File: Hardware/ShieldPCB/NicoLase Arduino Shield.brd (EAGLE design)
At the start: 54.3 x 62.2 mm, 19 parts, among them IC1 4050D, J1 ARDUINO_R3_SHIELD, U1 7432SE

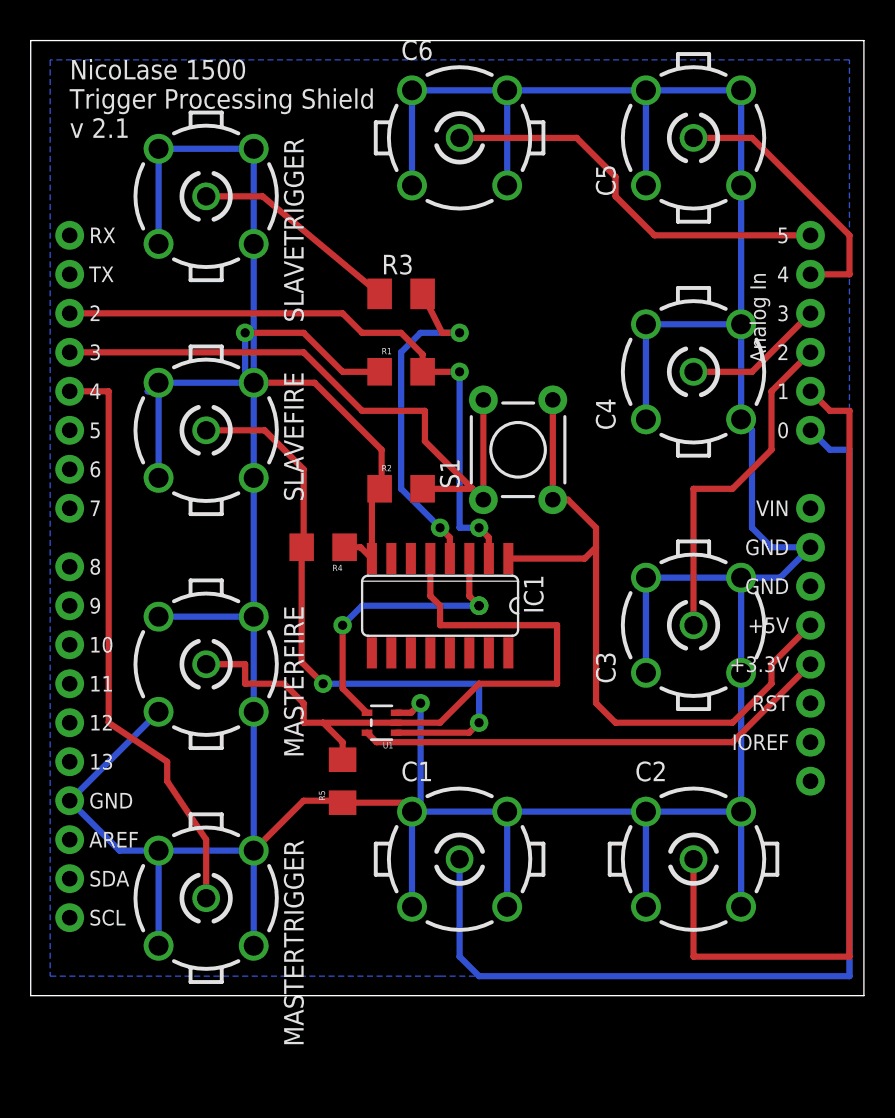
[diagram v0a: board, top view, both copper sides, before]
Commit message: Added ground plane and corrected minor layout issues.
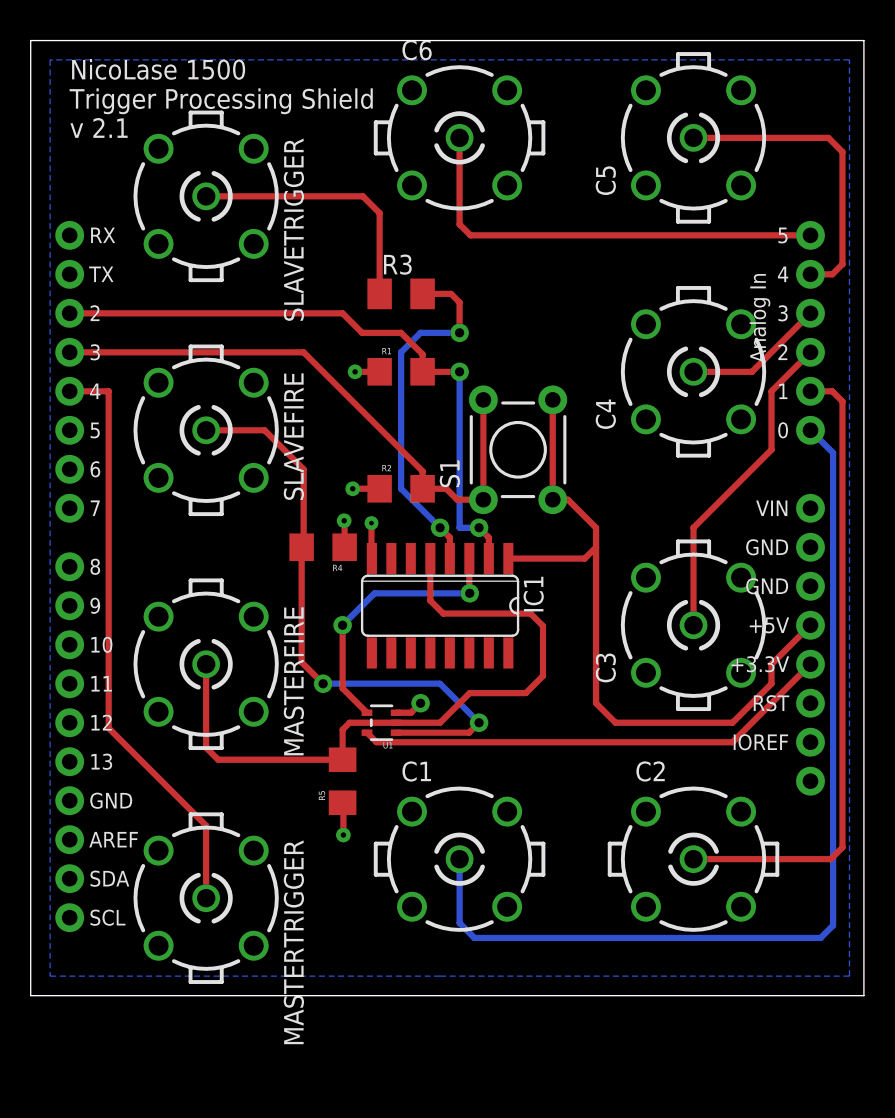
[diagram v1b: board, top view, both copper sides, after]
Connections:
- net N$2 renamed GND
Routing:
- net GND: track 331.7 -> 12.5 mm, vias 2 -> 6
- net N$4: track 55.1 -> 41.4 mm
- net N$3: track 69.6 -> 62.1 mm
- net N$13: track 42.8 -> 38.1 mm
- net N$11: track 13.6 -> 17.0 mm
- net N$8: track 26.2 -> 28.8 mm
- net N$7: track 17.9 -> 19.8 mm
- net N$26: track 40.4 -> 38.9 mm
- net N$5: track 22.4 -> 20.9 mm
- net N$10: track 19.1 -> 17.8 mm
- net SLAVEFIRE: track 46.0 -> 45.1 mm
- net N$15: track 23.1 -> 23.7 mm
- added copper zone on layer 16, net GND
- removed copper zone on layer 16, net N$20

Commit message: Added 0.1uF capacitors on power rails. Correcter minor schematic issues.
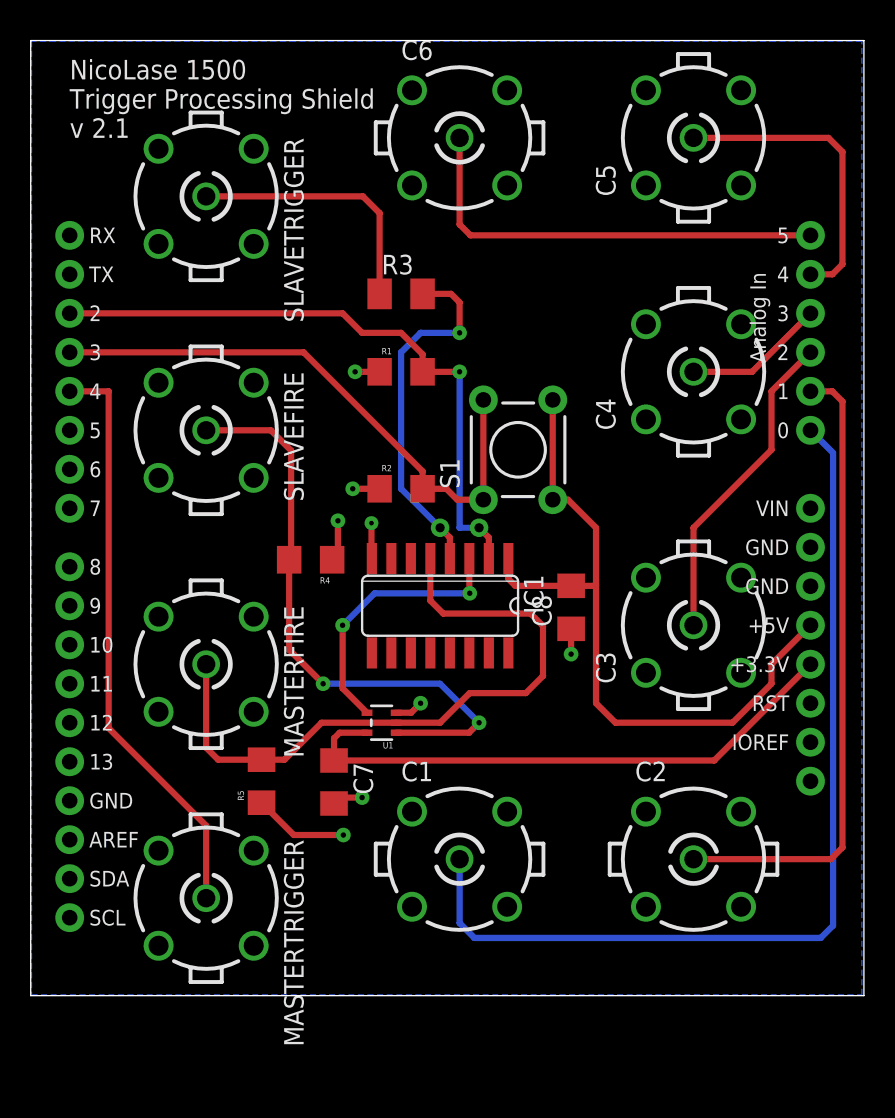
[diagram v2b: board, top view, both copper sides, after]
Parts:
- added C7, C8: 0.1uF, rcl:C1206
- moved R5 5.28 mm to (18.8, 21.6)
- moved R4 1.15 mm to (22.0, 36.0)
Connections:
- net GND: now also C7.2, C8.1
- net N$1: now also C7.1
- net N$16: now also C8.2
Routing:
- net GND: track 12.5 -> 21.1 mm, vias 6 -> 8
- net N$1: track 31.3 -> 37.4 mm
- net N$16: track 46.7 -> 48.0 mm
- net SLAVEFIRE: track 45.1 -> 44.0 mm

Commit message: Updated top silk.
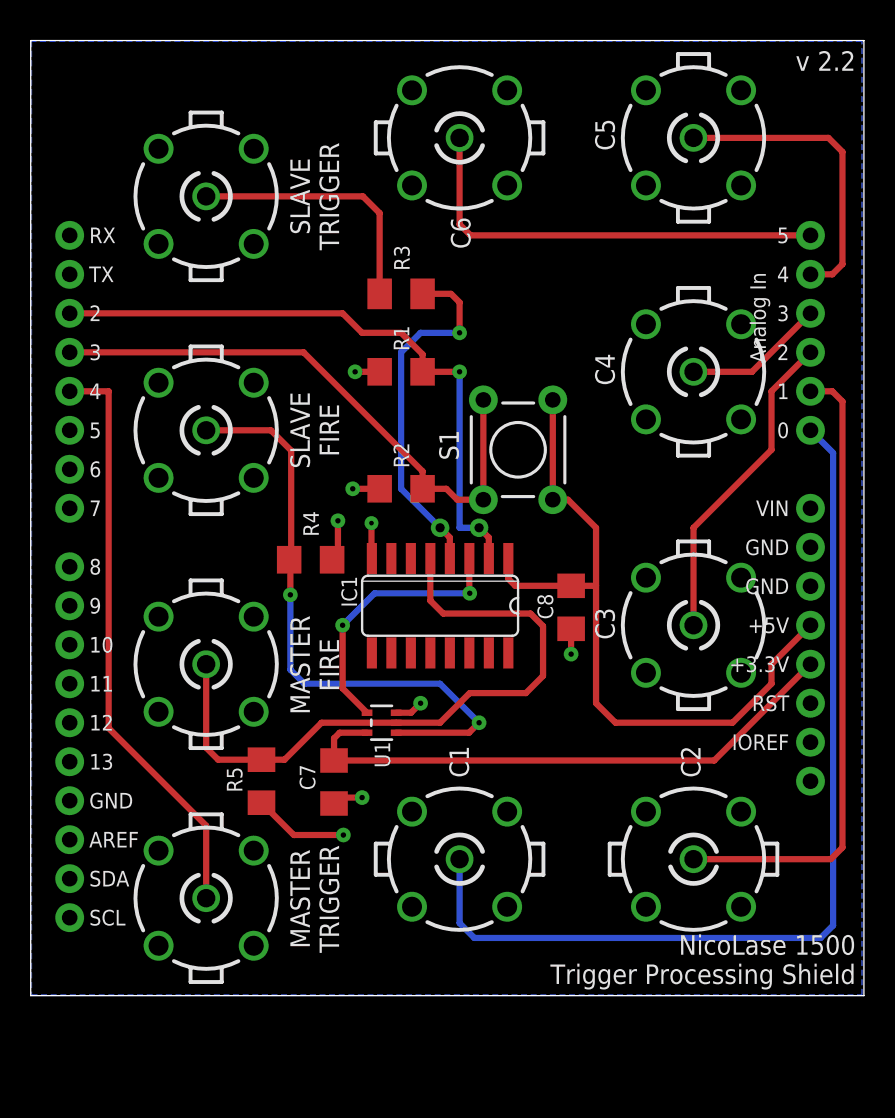
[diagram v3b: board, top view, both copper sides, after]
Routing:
- net N$26: track 39.1 -> 39.9 mm
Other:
- board text added: "MASTER FIRE"
- board text added: "MASTER TRIGGER"
- board text added: "NicoLase 1500 Trigger Processing Shield"
- board text added: "SLAVE FIRE"
- board text added: "SLAVE TRIGGER"
- board text added: "v 2.2"
- board text removed: "NicoLase 1500 Trigger Processing Shield v 2.1"

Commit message: Review filcarv pull request.  Update silkscreen and README terminology for primary/secondary fire/trigger lines.
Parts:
- renumbered MASTERFIRE to PRIMARYFIRE, MASTERTRIGGER to PRIMARYTRIGGER, SLAVEFIRE to 2NDARYFIRE, SLAVETRIGGER to 2NDARYTRIGGER
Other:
- board text added: "PRIMARY FIRE"
- board text added: "PRIMARY TRIGGER"
- board text added: "SECONDARY FIRE"
- board text added: "SECONDARY TRIGGER"
- board text removed: "MASTER FIRE"
- board text removed: "MASTER TRIGGER"
- board text removed: "SLAVE FIRE"
- board text removed: "SLAVE TRIGGER"
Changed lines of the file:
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@@
 <?xml version="1.0" encoding="utf-8"?>
 <!DOCTYPE eagle SYSTEM "eagle.dtd">
-<eagle version="9.5.1">
+<eagle version="9.0.1">
 <drawing>
 <settings>
@@
 <text x="57.5564" y="8.382" size="1.27" layer="21" font="vector" ratio="12" align="bottom-right">NicoLase 1500
 Trigger Processing Shield</text>
-<text x="20.7264" y="13.9192" size="1.27" layer="21" font="vector" ratio="15" rot="R90" align="top-center">MASTER
+<text x="20.7264" y="13.9192" size="1.27" layer="21" font="vector" ratio="15" rot="R90" align="top-center">PRIMARY
 TRIGGER</text>
-<text x="20.7264" y="29.1592" size="1.27" layer="21" font="vector" ratio="15" rot="R90" align="top-center">MASTER
+<text x="20.7264" y="29.1592" size="1.27" layer="21" font="vector" ratio="15" rot="R90" align="top-center">PRIMARY
 FIRE</text>
-<text x="20.7264" y="44.45" size="1.27" layer="21" font="vector" ratio="15" rot="R90" align="top-center">SLAVE
+<text x="20.7264" y="44.45" size="1.27" layer="21" font="vector" ratio="15" rot="R90" align="top-center">SECONDARY
 FIRE</text>
-<text x="20.7264" y="59.69" size="1.27" layer="21" font="vector" ratio="15" rot="R90" align="top-center">SLAVE
+<text x="20.7264" y="59.69" size="1.27" layer="21" font="vector" ratio="15" rot="R90" align="top-center">SECONDARY
 TRIGGER</text>
 <text x="57.5564" y="67.8688" size="1.27" layer="21" font="vector" ratio="12" align="bottom-right">v 2.2</text>
@@
 <param name="checkStop" value="0"/>
 <param name="checkValues" value="0"/>
-<param name="checkNames" value="1"/>
-<param name="checkWireStubs" value="1"/>
-<param name="checkPolygonWidth" value="0"/>
 <param name="useDiameter" value="13"/>
 <param name="maxErrors" value="50"/>
@@
 <attribute name="VALUE" x="34.544" y="33.655" size="1.27" layer="27" ratio="10" rot="R180"/>
 </element>
-<element name="MASTERFIRE" library="con-coax" package="B35N61" value="BN35N61" x="15.24" y="29.21" smashed="yes" rot="R270">
+<element name="PRIMARYFIRE" library="con-coax" package="B35N61" value="BN35N61" x="15.24" y="29.21" smashed="yes" rot="R270">
 <attribute name="MF" value="" x="15.24" y="29.21" size="1.778" layer="27" rot="R270" display="off"/>
 <attribute name="MPN" value="" x="15.24" y="29.21" size="1.778" layer="27" rot="R270" display="off"/>
@@
 <attribute name="NAME" x="30.4292" y="43.4848" size="1.27" layer="25" font="vector" ratio="15" rot="R270" align="bottom-center"/>
 </element>
-<element name="SLAVEFIRE" library="con-coax" package="B35N61" value="BN35N61" x="15.24" y="44.45" smashed="yes" rot="R270">
+<element name="2NDARYFIRE" library="con-coax" package="B35N61" value="BN35N61" x="15.24" y="44.45" smashed="yes" rot="R270">
 <attribute name="MF" value="" x="15.24" y="44.45" size="1.778" layer="27" rot="R270" display="off"/>
 <attribute name="MPN" value="" x="15.24" y="44.45" size="1.778" layer="27" rot="R270" display="off"/>
@@
 <attribute name="VALUE" x="8.89" y="48.26" size="1.27" layer="27" rot="R270"/>
 </element>
-<element name="SLAVETRIGGER" library="con-coax" package="B35N61" value="BN35N61" x="15.24" y="59.69" smashed="yes" rot="R270">
+<element name="2NDARYTRIGGER" library="con-coax" package="B35N61" value="BN35N61" x="15.24" y="59.69" smashed="yes" rot="R270">
 <attribute name="MF" value="" x="15.24" y="59.69" size="1.778" layer="27" rot="R270" display="off"/>
 <attribute name="MPN" value="" x="15.24" y="59.69" size="1.778" layer="27" rot="R270" display="off"/>
@@
 <attribute name="VALUE" x="27.432" y="27.051" size="0.4064" layer="27" rot="R180"/>
 </element>
-<element name="MASTERTRIGGER" library="con-coax" package="B35N61" value="BN35N61" x="15.24" y="13.97" smashed="yes" rot="R270">
+<element name="PRIMARYTRIGGER" library="con-coax" package="B35N61" value="BN35N61" x="15.24" y="13.97" smashed="yes" rot="R270">
 <attribute name="MF" value="" x="15.24" y="13.97" size="1.778" layer="27" rot="R270" display="off"/>
 <attribute name="MPN" value="" x="15.24" y="13.97" size="1.778" layer="27" rot="R270" display="off"/>
@@
 <contactref element="R5" pad="2"/>
 <contactref element="IC1" pad="5"/>
-<contactref element="MASTERFIRE" pad="1"/>
+<contactref element="PRIMARYFIRE" pad="1"/>
 <wire x1="30.48" y1="25.4" x2="32.4104" y2="27.3304" width="0.4064" layer="1"/>
 <wire x1="27.62" y1="25.4" x2="22.7584" y2="25.4" width="0.4064" layer="1"/>
@@
 <signal name="GND">
 <contactref element="IC1" pad="8"/>
-<contactref element="SLAVETRIGGER" pad="2"/>
-<contactref element="SLAVETRIGGER" pad="3"/>
-<contactref element="SLAVETRIGGER" pad="4"/>
-<contactref element="SLAVETRIGGER" pad="5"/>
-<contactref element="SLAVEFIRE" pad="2"/>
-<contactref element="SLAVEFIRE" pad="3"/>
-<contactref element="SLAVEFIRE" pad="4"/>
-<contactref element="SLAVEFIRE" pad="5"/>
-<contactref element="MASTERFIRE" pad="2"/>
-<contactref element="MASTERFIRE" pad="3"/>
-<contactref element="MASTERFIRE" pad="4"/>
-<contactref element="MASTERFIRE" pad="5"/>
+<contactref element="2NDARYTRIGGER" pad="2"/>
+<contactref element="2NDARYTRIGGER" pad="3"/>
+<contactref element="2NDARYTRIGGER" pad="4"/>
+<contactref element="2NDARYTRIGGER" pad="5"/>
+<contactref element="2NDARYFIRE" pad="2"/>
+<contactref element="2NDARYFIRE" pad="3"/>
+<contactref element="2NDARYFIRE" pad="4"/>
+<contactref element="2NDARYFIRE" pad="5"/>
+<contactref element="PRIMARYFIRE" pad="2"/>
+<contactref element="PRIMARYFIRE" pad="3"/>
+<contactref element="PRIMARYFIRE" pad="4"/>
+<contactref element="PRIMARYFIRE" pad="5"/>
 <contactref element="U1" pad="3"/>
 <contactref element="R1" pad="1"/>
@@
 <contactref element="C2" pad="5"/>
 <contactref element="C2" pad="2"/>
-<contactref element="MASTERTRIGGER" pad="4"/>
-<contactref element="MASTERTRIGGER" pad="3"/>
-<contactref element="MASTERTRIGGER" pad="5"/>
-<contactref element="MASTERTRIGGER" pad="2"/>
+<contactref element="PRIMARYTRIGGER" pad="4"/>
+<contactref element="PRIMARYTRIGGER" pad="3"/>
+<contactref element="PRIMARYTRIGGER" pad="5"/>
+<contactref element="PRIMARYTRIGGER" pad="2"/>
 <contactref element="J1" pad="GND@2"/>
 <contactref element="J1" pad="GND@1"/>
@@
 </signal>
 <signal name="N$11">
-<contactref element="SLAVETRIGGER" pad="1"/>
+<contactref element="2NDARYTRIGGER" pad="1"/>
 <contactref element="R3" pad="1"/>
 <wire x1="26.54" y1="58.6008" x2="26.54" y2="53.34" width="0.4064" layer="1"/>
@@
 </signal>
 <signal name="N$19">
-<contactref element="MASTERTRIGGER" pad="1"/>
+<contactref element="PRIMARYTRIGGER" pad="1"/>
 <contactref element="J1" pad="D4"/>
 <wire x1="6.35" y1="46.99" x2="8.89" y2="46.99" width="0.4064" layer="1"/>
@@
 <contactref element="R4" pad="2"/>
 <contactref element="U1" pad="1"/>
-<contactref element="SLAVEFIRE" pad="1"/>
+<contactref element="2NDARYFIRE" pad="1"/>
 <wire x1="15.24" y1="44.45" x2="19.4564" y2="44.45" width="0.4064" layer="1"/>
 <wire x1="19.4564" y1="44.45" x2="20.7772" y2="43.1292" width="0.4064" layer="1"/>
@@
 </signal>
 </signals>
-<mfgpreviewcolors>
-<mfgpreviewcolor name="soldermaskcolor" color="0xC8008000"/>
-<mfgpreviewcolor name="silkscreencolor" color="0xFFFEFEFE"/>
-<mfgpreviewcolor name="backgroundcolor" color="0xFF282828"/>
-<mfgpreviewcolor name="coppercolor" color="0xFFFFBF00"/>
-<mfgpreviewcolor name="substratecolor" color="0xFF786E46"/>
-</mfgpreviewcolors>
 </board>
 </drawing>
